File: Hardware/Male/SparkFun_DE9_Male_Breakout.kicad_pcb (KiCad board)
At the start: 2 copper layers, 22.9 x 31.8 mm, 43 parts, among them J1 Conn_01x01, J2 Conn_01x09, J4 Conn_01x01, J5 DE9-Male

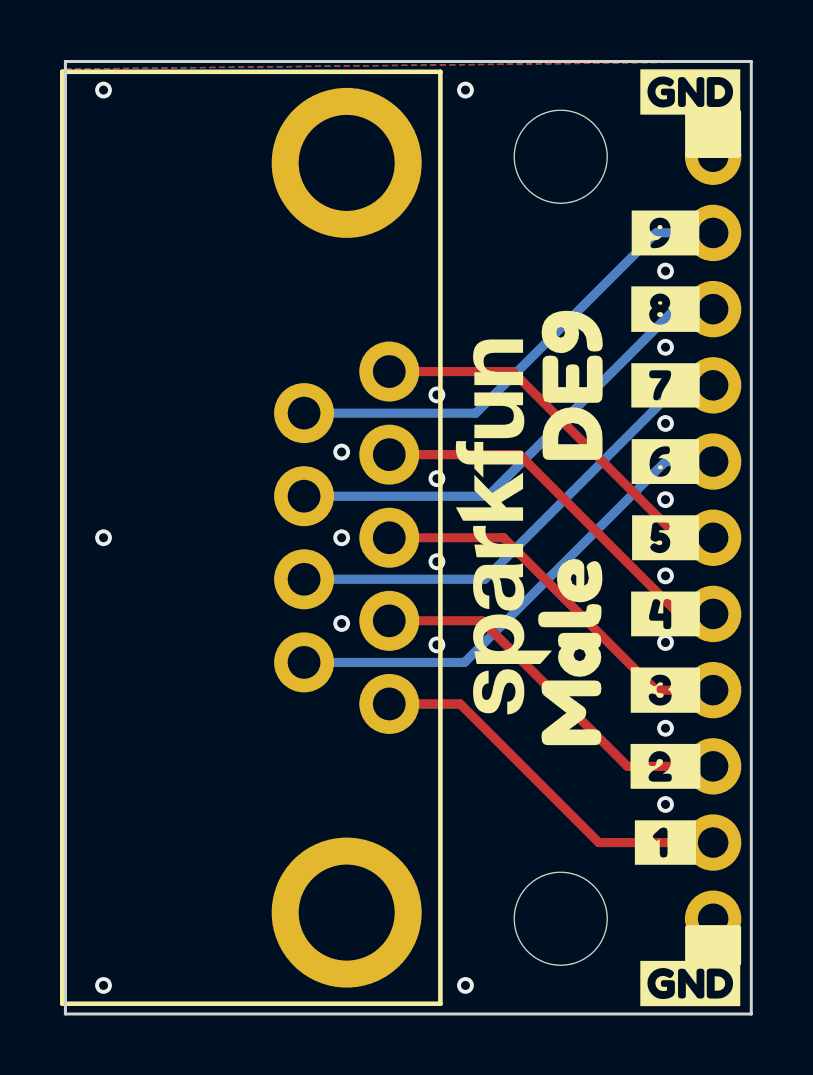
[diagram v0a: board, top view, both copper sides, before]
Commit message: Removes the local symbols/footprints, moves designs to Hardware folder
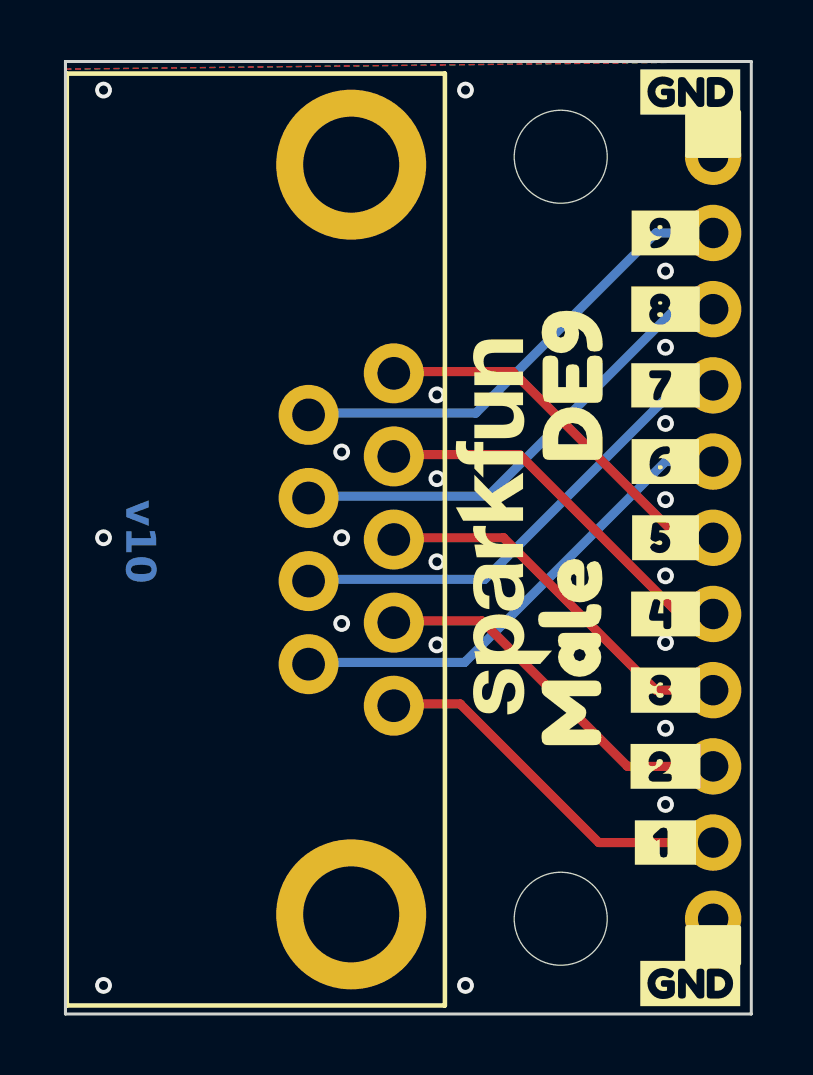
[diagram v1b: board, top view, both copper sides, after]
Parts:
- removed J5: DE9-Male, DE9-Footprint:DE9
- added J3: DE9 Male, SparkFun-Connector:DE9_Male, F.Cu at (126.5, 108.6)
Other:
- board text added: "v10"
